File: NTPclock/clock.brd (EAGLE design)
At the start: 115 x 85 mm, 26 parts, among them IC1 MAX7219CNG

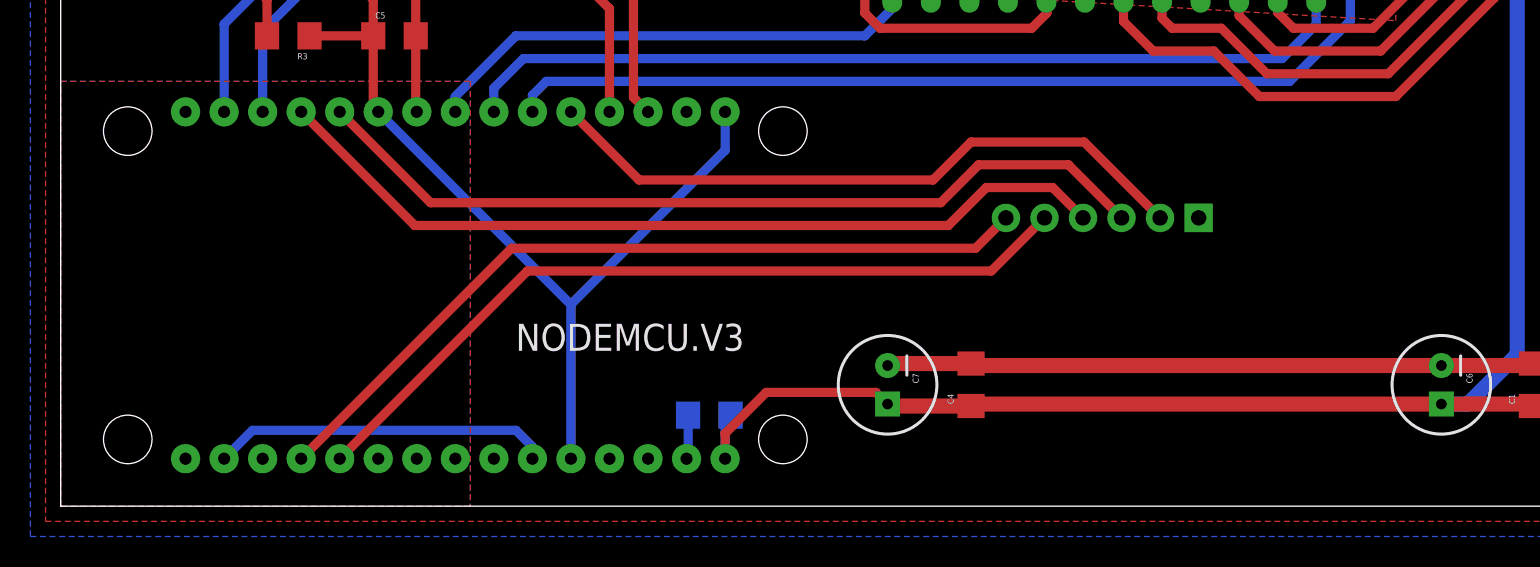
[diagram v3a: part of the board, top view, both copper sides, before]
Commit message: Silkscreen changes
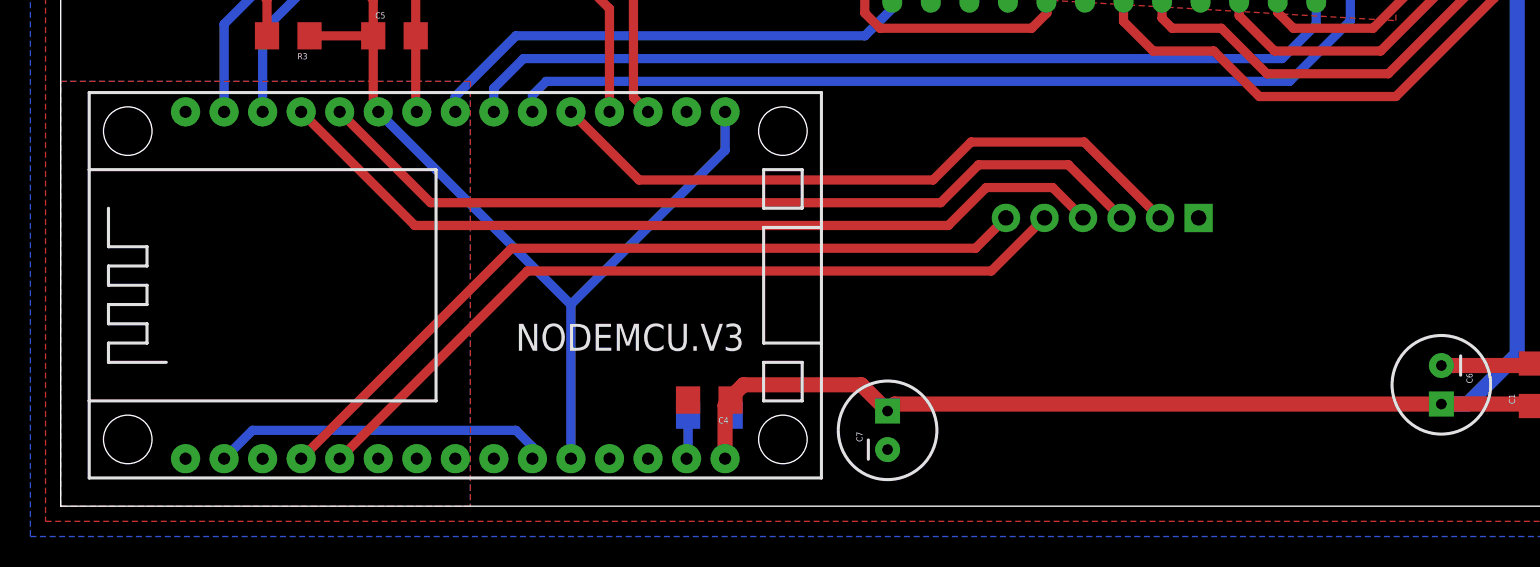
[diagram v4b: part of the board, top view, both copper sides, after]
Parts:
- NODEMCU.V3: value (none) -> ESP12E_DEVKIT
- moved C4 17.3 mm to (42.8, 7.00), turned to 180 degrees
- moved C7 3.00 mm to (54.5, 5.00), turned to 90 degrees
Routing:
- net GND: track 121.3 -> 84.7 mm
- net VCC: track 140.0 -> 141.8 mm
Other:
- board text added: "-"
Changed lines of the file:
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@@
 SQL
 32K</text>
-<text x="89.5" y="5.75" size="1.778" layer="22" rot="MR0">+</text>
-<text x="57" y="6" size="1.778" layer="22" rot="MR0">+</text>
-<text x="90.5" y="38.25" size="1.778" layer="22" rot="MR0">+</text>
+<text x="93.25" y="5.75" size="1.778" layer="22" rot="MR0">+</text>
+<text x="56.75" y="6" size="1.778" layer="22" rot="MR0">+</text>
+<text x="87" y="38.25" size="1.778" layer="22" rot="MR0">+</text>
 <wire x1="115" y1="35" x2="113" y2="33" width="0" layer="20" curve="-90"/>
 <wire x1="113" y1="33" x2="109" y2="33" width="0" layer="20"/>
@@
 TX</text>
 <rectangle x1="41" y1="24" x2="42" y2="25" layer="41"/>
+<text x="107.25" y="5.5" size="1.778" layer="22" rot="MR0">+</text>
+<text x="107.5" y="10.5" size="1.778" layer="22" rot="MR270">-</text>
 </plain>
 <attributes>
@@
 </autorouter>
 <elements>
-<element name="NODEMCU.V3" library="NODEMCUv1" package="ESP12E_DEVKIT" value="" x="26.01" y="14.56" rot="R90"/>
+<element name="NODEMCU.V3" library="NODEMCUv1" package="ESP12E_DEVKIT" value="ESP12E_DEVKIT" x="26.01" y="14.56" rot="R90"/>
 <element name="IC1" library="max7219" package="DIL24-3" value="MAX7219CNG" x="68.78" y="37.65">
 <attribute name="MF" value="MAXIM" x="68.78" y="37.65" size="1.778" layer="27" display="off"/>
@@
 <element name="C2" library="SparkFun-Capacitors" package="1206" value="" x="42.75" y="6" rot="MR0"/>
 <element name="C3" library="SparkFun-Capacitors" package="1206" value="0.1μF" x="65" y="37.5" rot="MR0"/>
-<element name="C4" library="SparkFun-Capacitors" package="1206" value="" x="60" y="8" rot="R90"/>
+<element name="C4" library="SparkFun-Capacitors" package="1206" value="" x="42.75" y="7" rot="R180"/>
 <element name="C5" library="SparkFun-Capacitors" package="1206" value="" x="22" y="31"/>
 <element name="C6" library="SparkFun-Capacitors" package="CPOL-RADIAL-100UF-25V" value="470μF" x="91" y="8" rot="R270"/>
-<element name="C7" library="SparkFun-Capacitors" package="CPOL-RADIAL-100UF-25V" value="" x="54.5" y="8" rot="R270"/>
+<element name="C7" library="SparkFun-Capacitors" package="CPOL-RADIAL-100UF-25V" value="" x="54.5" y="5" rot="R90"/>
 <element name="C8" library="SparkFun-Capacitors" package="CPOL-RADIAL-100UF-25V" value="10μF" x="88" y="37.75" rot="R90"/>
 <element name="POWER" library="SparkFun-Connectors" package="JST-2-PTH-VERT" value="" x="103" y="8" rot="MR270"/>
@@
 <wire x1="97" y1="9.4" x2="96.87" y2="9.27" width="1" layer="1"/>
 <wire x1="96.87" y1="9.27" x2="91" y2="9.27" width="1" layer="1"/>
-<wire x1="60" y1="9.4" x2="54.63" y2="9.4" width="1" layer="1"/>
-<wire x1="54.63" y1="9.4" x2="54.5" y2="9.27" width="1" layer="1"/>
-<wire x1="91" y1="9.27" x2="60.13" y2="9.27" width="1" layer="1"/>
-<wire x1="60.13" y1="9.27" x2="60" y2="9.4" width="1" layer="1"/>
 <contactref element="BUTTONS" pad="1"/>
 <wire x1="10.77" y1="3.13" x2="12.64" y2="5" width="0.6096" layer="16"/>
@@
 <wire x1="68.98" y1="39.02" x2="67.51" y2="40.49" width="1.016" layer="1"/>
 <wire x1="67.51" y1="40.49" x2="67.51" y2="41.46" width="1.016" layer="1"/>
-<wire x1="46.5" y1="7.5" x2="43.79" y2="4.79" width="0.6096" layer="1"/>
-<wire x1="43.79" y1="4.79" x2="43.79" y2="3.13" width="0.6096" layer="1"/>
 <wire x1="66.4" y1="37.5" x2="66.4" y2="38.4" width="0.6096" layer="16"/>
 <wire x1="66.4" y1="38.4" x2="67.51" y2="39.51" width="0.6096" layer="16"/>
@@
 <wire x1="97" y1="6.6" x2="96.87" y2="6.73" width="1" layer="1"/>
 <wire x1="96.87" y1="6.73" x2="91" y2="6.73" width="1" layer="1"/>
-<wire x1="91" y1="6.73" x2="60.13" y2="6.73" width="1" layer="1"/>
-<wire x1="60.13" y1="6.73" x2="60" y2="6.6" width="1" layer="1"/>
-<wire x1="60" y1="6.6" x2="54.63" y2="6.6" width="1" layer="1"/>
-<wire x1="54.63" y1="6.6" x2="54.5" y2="6.73" width="1" layer="1"/>
-<wire x1="46.5" y1="7.5" x2="53.73" y2="7.5" width="0.6096" layer="1"/>
-<wire x1="53.73" y1="7.5" x2="54.5" y2="6.73" width="0.6096" layer="1"/>
+<wire x1="44.15" y1="7" x2="43.79" y2="6.64" width="1" layer="1"/>
+<wire x1="43.79" y1="6.64" x2="43.79" y2="3.13" width="1" layer="1"/>
+<wire x1="52.77" y1="8" x2="45" y2="8" width="1" layer="1"/>
+<wire x1="45" y1="8" x2="44.15" y2="7.15" width="1" layer="1"/>
+<wire x1="44.15" y1="7.15" x2="44.15" y2="7" width="1" layer="1"/>
+<wire x1="91" y1="6.73" x2="54.96" y2="6.73" width="1" layer="1"/>
+<wire x1="54.96" y1="6.73" x2="54.5" y2="6.27" width="1" layer="1"/>
+<wire x1="52.77" y1="8" x2="54.5" y2="6.27" width="1" layer="1"/>
 </signal>
 <signal name="3.3V">
